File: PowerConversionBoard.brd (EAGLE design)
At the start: 152.4 x 101.6 mm, 46 parts, among them U1 LM2678, U2 LM2678

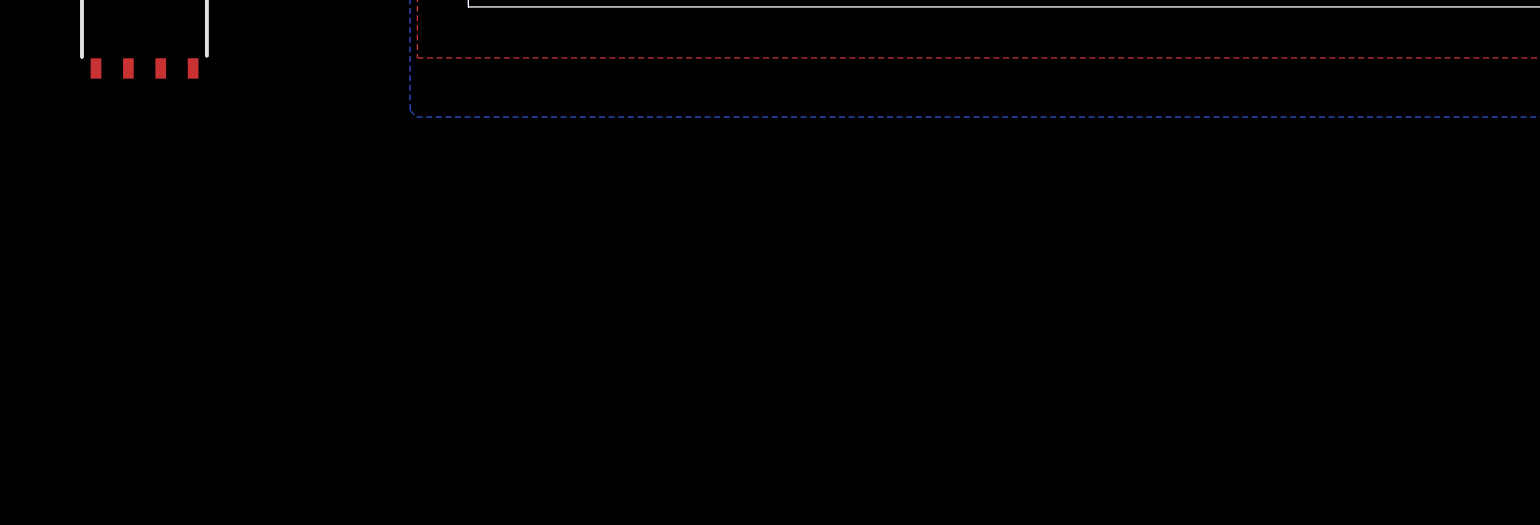
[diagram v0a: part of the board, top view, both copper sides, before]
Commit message: added the power ditribution connector
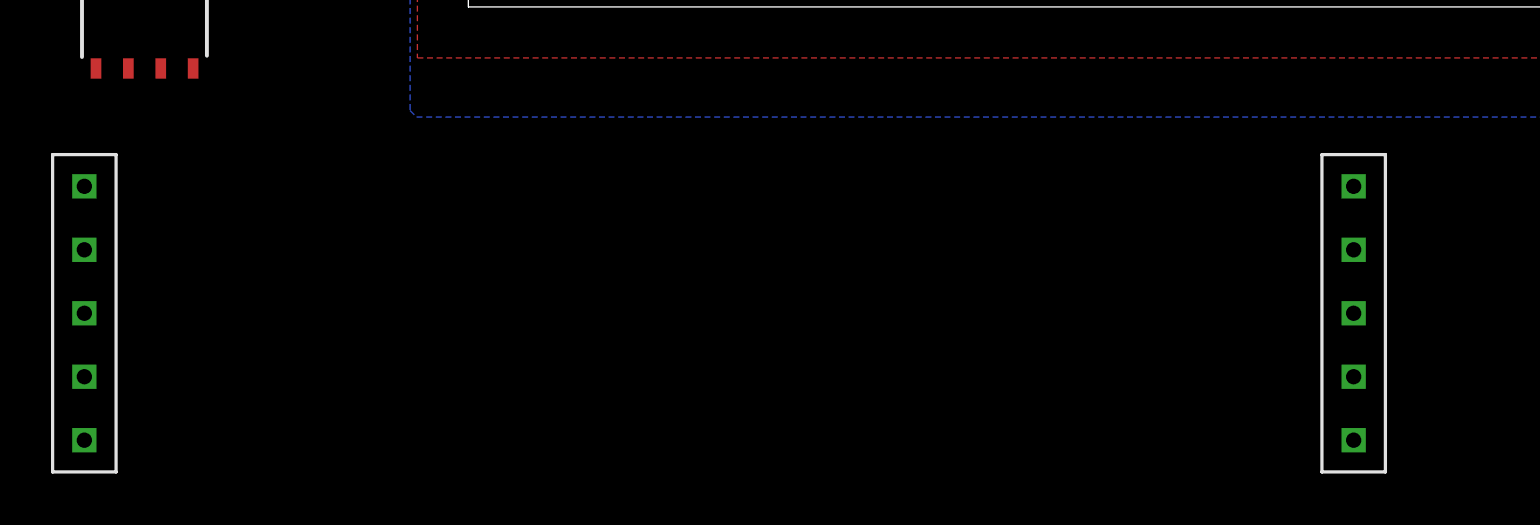
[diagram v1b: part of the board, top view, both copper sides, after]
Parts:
- added U$4: DIST_TO_CONV, Dist_To_Conv_Connector:DIST_TO_CONV
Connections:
- net +3.3V: now also U$4.3V
- net +48V: now also U$4.48V
- net +5V_3.3V: now also U$4.5V_1, U$4.5V_2, U$4.5V_3, U$4.5V_4
- net GND: now also U$4.GND_1, U$4.GND_2, U$4.GND_3, U$4.GND_4
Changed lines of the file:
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@@
 <attribute name="VALUE" x="-15.875" y="-4.953" size="1.778" layer="27"/>
 </element>
+<element name="U$4" library="Dist_To_Conv_Connector" package="DIST_TO_CONV" value="DIST_TO_CONV" x="-12.573" y="-9.525" smashed="yes"/>
 </elements>
 <signals>
@@
 <via x="105.41" y="36.576" extent="1-16" drill="0.9"/>
 <contactref element="U$6" pad="3"/>
+<contactref element="U$4" pad="GND_3"/>
+<contactref element="U$4" pad="GND_4"/>
+<contactref element="U$4" pad="GND_1"/>
+<contactref element="U$4" pad="GND_2"/>
 <wire x1="141.0716" y1="82.7906" x2="146.2532" y2="81.6356" width="0" layer="19" extent="1-1"/>
 <wire x1="132.715" y1="81.3698" x2="141.0716" y2="82.7906" width="0" layer="19" extent="1-1"/>
@@
 <wire x1="56.896" y1="3.302" x2="41.656" y2="3.048" width="0" layer="19" extent="1-1"/>
 <wire x1="-12.065" y1="-2.413" x2="3.81" y2="4.318" width="0" layer="19" extent="1-1"/>
+<wire x1="-15.0622" y1="-14.5034" x2="-12.065" y2="-2.413" width="0" layer="19" extent="1-1"/>
+<wire x1="-15.0622" y1="-16.9926" x2="-15.0622" y2="-14.5034" width="0" layer="19" extent="1-1"/>
+<wire x1="34.7218" y1="-14.5034" x2="33.528" y2="3.302" width="0" layer="19" extent="1-1"/>
+<wire x1="34.7218" y1="-16.9926" x2="34.7218" y2="-14.5034" width="0" layer="19" extent="1-1"/>
 <wire x1="78.232" y1="3.302" x2="56.896" y2="3.302" width="0" layer="19" extent="1-1"/>
 </signal>
@@
 <contactref element="U$6" pad="1"/>
 <contactref element="U$6" pad="2"/>
+<contactref element="U$4" pad="3V"/>
 <wire x1="-13.335" y1="-2.413" x2="124.3312" y2="84.9612" width="0" layer="19" extent="1-1"/>
 <wire x1="-14.605" y1="-2.413" x2="-13.335" y2="-2.413" width="0" layer="19" extent="1-1"/>
+<wire x1="-15.0622" y1="-7.0358" x2="-14.605" y2="-2.413" width="0" layer="19" extent="1-1"/>
 </signal>
 <signal name="N$2">
@@
 <contactref element="U$6" pad="8"/>
 <contactref element="U$6" pad="5"/>
+<contactref element="U$4" pad="5V_1"/>
+<contactref element="U$4" pad="5V_2"/>
+<contactref element="U$4" pad="5V_3"/>
+<contactref element="U$4" pad="5V_4"/>
 <wire x1="96.012" y1="96.012" x2="103.0224" y2="96.393" width="0" layer="19" extent="1-1"/>
 <wire x1="83.1986" y1="91.5416" x2="96.012" y2="96.012" width="0" layer="19" extent="1-1"/>
-<wire x1="-10.795" y1="2.787" x2="46.9138" y2="83.4898" width="0" layer="19" extent="1-1"/>
+<wire x1="34.7218" y1="-9.525" x2="46.9138" y2="83.4898" width="0" layer="19" extent="1-1"/>
+<wire x1="34.7218" y1="-12.0142" x2="34.7218" y2="-9.525" width="0" layer="19" extent="1-1"/>
+<wire x1="-10.795" y1="2.787" x2="34.7218" y2="-9.525" width="0" layer="19" extent="1-1"/>
 <wire x1="-14.605" y1="2.787" x2="-10.795" y2="2.787" width="0" layer="19" extent="1-1"/>
+<wire x1="-15.0622" y1="-9.525" x2="-14.605" y2="2.787" width="0" layer="19" extent="1-1"/>
+<wire x1="-15.0622" y1="-12.0142" x2="-15.0622" y2="-9.525" width="0" layer="19" extent="1-1"/>
 </signal>
 <signal name="N$3">
@@
 <wire x1="52.07" y1="85.852" x2="44.45" y2="93.472" width="1.27" layer="16"/>
 <wire x1="44.45" y1="93.472" x2="43.18" y2="93.472" width="1.27" layer="16"/>
+<contactref element="U$4" pad="48V"/>
 <wire x1="43.18" y1="93.472" x2="42.9514" y2="91.7058" width="0" layer="19" extent="16-16"/>
 <wire x1="38.227" y1="93.8726" x2="43.18" y2="93.472" width="0" layer="19" extent="16-16"/>
@@
 <wire x1="4.6736" y1="96.8756" x2="10.2616" y2="96.6352" width="0" layer="19" extent="1-1"/>
 <wire x1="4.9784" y1="89.3572" x2="4.6736" y2="96.8756" width="0" layer="19" extent="1-1"/>
+<wire x1="34.7218" y1="-7.0358" x2="51.9938" y2="83.4898" width="0" layer="19" extent="1-1"/>
 </signal>
 </signals>

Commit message: Align schematic to 0.1 in. Create board with dimension
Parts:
- U$2, U$7: value HCM1305 -> HCMA1305; device HCM1305:HCM1305 -> Inductor_15uH - hcma1305:HCMA1305
- moved D1 221.0 mm to (-69.8, 76.2), turned to 0 degrees
- moved +3.3V 210.3 mm to (-57.1, 47.0)
- moved R2 209.7 mm to (-58.4, 76.2), turned to 0 degrees
- moved +5V 209.3 mm to (-63.5, 47.0)
- moved R3 204.5 mm to (-62.2, 76.2), turned to 0 degrees
- moved GND3 177.2 mm to (-29.2, 57.1)
- moved R4 174.7 mm to (-41.9, 76.2), turned to 0 degrees
- moved 5V_3.3 173.0 mm to (-69.8, 47.0)
- moved U$13 172.1 mm to (-36.8, 57.1), turned to 0 degrees
- moved 5V 171.5 mm to (-25.4, 47.0)
- moved +3.3 166.1 mm to (-19.1, 47.0)
- moved R1 163.8 mm to (-54.6, 76.2), turned to 0 degrees
- moved 5V_3.3_TP 163.5 mm to (-48.3, 34.3)
- moved D3 156.3 mm to (-15.2, 82.5), turned to 0 degrees
- moved C12 153.0 mm to (-67.3, 57.1), turned to 0 degrees
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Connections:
- net +12V renamed N$11
- net +5V: now also U$2.P$2; no longer U$2.2, U1.6
- net +5V_3.3V: now also U$7.P$2; no longer U$7.2
- net N$1: now also U$2.P$1, U1.6; no longer U$2.1
- net N$7: now also U$7.P$1; no longer U$7.1
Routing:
- net +5V: track 116.5 -> 0.00 mm, vias 7 -> 0
- net +5V_3.3V: track 54.9 -> 0.00 mm
- net +3.3V: track 34.7 -> 0.00 mm, vias 5 -> 0
- net N$1: track 33.5 -> 0.00 mm
- net GND: track 28.2 -> 0.00 mm, vias 67 -> 0
- net N$7: track 28.0 -> 0.00 mm
- net +48V: track 15.8 -> 0.00 mm, vias 2 -> 0
- net N$2: track 9.97 -> 0.00 mm
- net N$14: track 9.64 -> 0.00 mm
- net N$11: track 9.27 -> 0.00 mm, vias 1 -> 0
- net N$5: track 2.95 -> 0.00 mm
- net N$6: track 2.88 -> 0.00 mm
- net N$10: track 2.87 -> 0.00 mm
- net N$8: track 2.24 -> 0.00 mm
- net N$4: track 1.93 -> 0.00 mm
- removed copper zone on layer 16, net +3.3V
- removed copper zone on layer 1, net +5V
- removed copper zone on layer 16, net +5V
- removed copper zone on layer 1, net +5V_3.3V
- removed copper zone on layer 1, net CUT
- removed copper zone on layer 16, net CUT
- removed copper zone on layer 16, net CUTG
- removed copper zone on layer 1, net GND
- removed copper zone on layer 16, net GND
- removed copper zone on layer 1, net GNDCUT
- removed copper zone on layer 16, net N$11
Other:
- board size 152.4 x 101.6 mm -> 72.4 x 71.1 mm
- board text removed: "Power Conversion v1 Guillermo Martinez Erin Park Ryan Pearson Cynthia Zatlokowicz"
- board text removed: "owo"

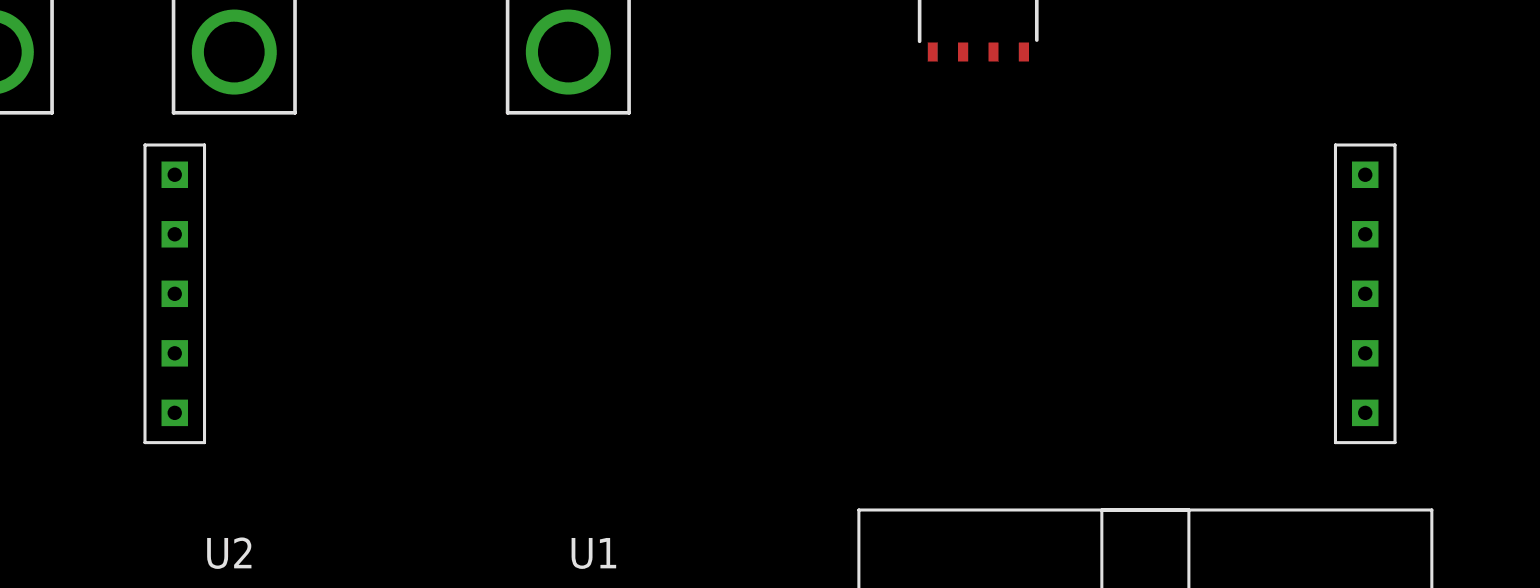
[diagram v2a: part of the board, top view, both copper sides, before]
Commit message: Added the connector to the distribution board
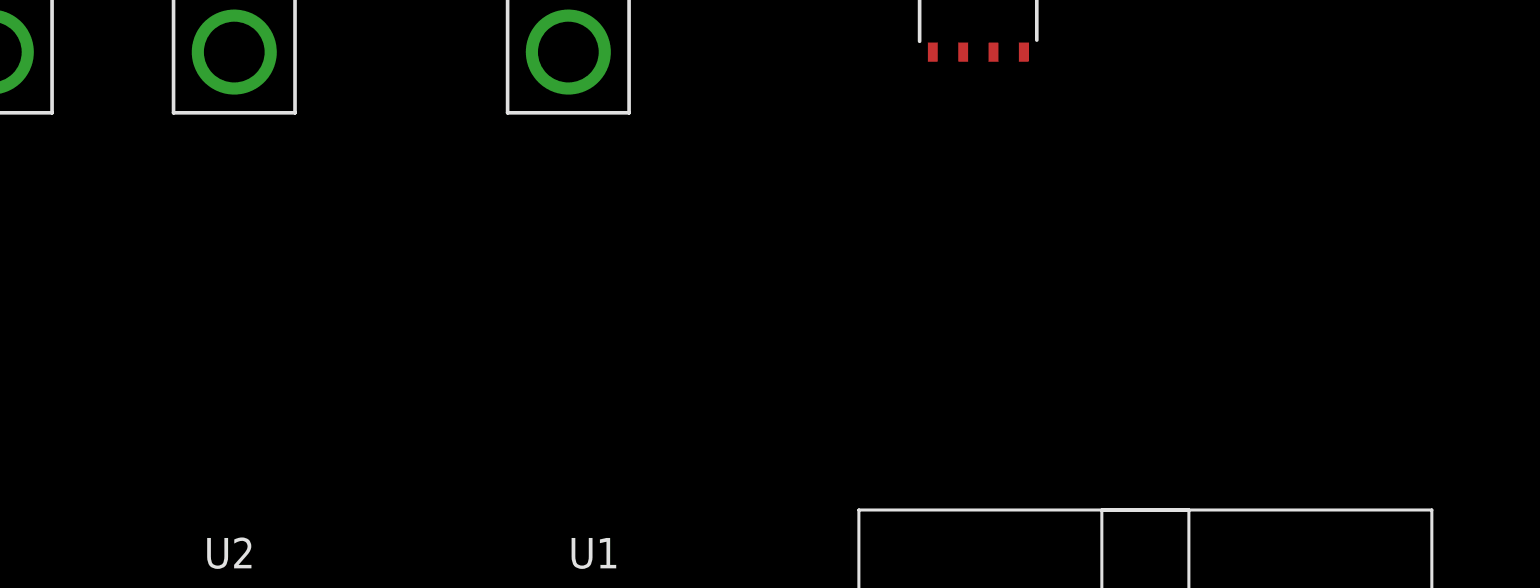
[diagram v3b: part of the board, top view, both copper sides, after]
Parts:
- removed U$4: DIST_TO_CONV, Dist_To_Conv_Connector:DIST_TO_CONV
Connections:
- net +3.3V: no longer U$4.3V
- net +48V: no longer U$4.48V
- net +5V_3.3V: no longer U$4.5V_1, U$4.5V_2, U$4.5V_3, U$4.5V_4
- net GND: no longer U$4.GND_1, U$4.GND_2, U$4.GND_3, U$4.GND_4
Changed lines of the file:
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@@
 <attribute name="NAME" x="-47.29" y="50.69" size="1.27" layer="25"/>
 </element>
-<element name="U$4" library="Dist_To_Conv_Connector" package="DIST_TO_CONV" value="DIST_TO_CONV" x="-62.23" y="26.67" smashed="yes"/>
 <element name="U$6" library="5-33Regulator" package="VOLTAGEREGULATOR" value="5-33REGULATOR" x="-33.02" y="34.29" smashed="yes">
 <attribute name="NAME" x="-34.29" y="40.64" size="1.778" layer="25"/>
@@
 <contactref element="D1" pad="C"/>
 <contactref element="D2" pad="C"/>
-<contactref element="U$4" pad="GND_3"/>
-<contactref element="U$4" pad="GND_4"/>
-<contactref element="U$4" pad="GND_1"/>
-<contactref element="U$4" pad="GND_2"/>
 <contactref element="C12" pad="-"/>
 <contactref element="U$1" pad="P$1"/>
@@
 <wire x1="-68.973" y1="76.2" x2="-61.55" y2="71.12" width="0" layer="19" extent="1-1"/>
 <wire x1="-72.783" y1="76.2" x2="-68.973" y2="76.2" width="0" layer="19" extent="1-1"/>
-<wire x1="-14.9352" y1="21.6916" x2="-30.48" y2="34.29" width="0" layer="19" extent="1-1"/>
-<wire x1="-14.9352" y1="19.2024" x2="-14.9352" y2="21.6916" width="0" layer="19" extent="1-1"/>
 <wire x1="-62.23" y1="34.29" x2="-42.91" y2="44.705" width="0" layer="19" extent="1-1"/>
-<wire x1="-64.7192" y1="21.6916" x2="-62.23" y2="34.29" width="0" layer="19" extent="1-1"/>
-<wire x1="-64.7192" y1="19.2024" x2="-64.7192" y2="21.6916" width="0" layer="19" extent="1-1"/>
-<wire x1="-58.42" y1="6.35" x2="-64.7192" y2="19.2024" width="0" layer="19" extent="1-1"/>
+<wire x1="-58.42" y1="6.35" x2="-62.23" y2="34.29" width="0" layer="19" extent="1-1"/>
 <wire x1="-50.0888" y1="6.35" x2="-58.42" y2="6.35" width="0" layer="19" extent="1-1"/>
 <wire x1="-43.18" y1="6.35" x2="-50.0888" y2="6.35" width="0" layer="19" extent="1-1"/>
@@
 <contactref element="+3.3V" pad="P$1"/>
 <contactref element="+3.3" pad="P$1"/>
-<contactref element="U$4" pad="3V"/>
-<wire x1="-57.15" y1="46.99" x2="-64.7192" y2="29.1592" width="0" layer="19" extent="1-1"/>
-<wire x1="-37.63" y1="57.15" x2="-57.15" y2="46.99" width="0" layer="19" extent="1-1"/>
-<wire x1="-19.05" y1="46.99" x2="-37.63" y2="57.15" width="0" layer="19" extent="1-1"/>
 <wire x1="-31.75" y1="34.29" x2="-19.05" y2="46.99" width="0" layer="19" extent="1-1"/>
 <wire x1="-33.02" y1="34.29" x2="-31.75" y2="34.29" width="0" layer="19" extent="1-1"/>
+<wire x1="-37.63" y1="57.15" x2="-19.05" y2="46.99" width="0" layer="19" extent="1-1"/>
+<wire x1="-57.15" y1="46.99" x2="-37.63" y2="57.15" width="0" layer="19" extent="1-1"/>
 <wire x1="-61.38" y1="76.2" x2="-57.15" y2="46.99" width="0" layer="19" extent="1-1"/>
 </signal>
@@
 <contactref element="5V_3.3" pad="P$1"/>
 <contactref element="5V_3.3_TP" pad="P$1"/>
-<contactref element="U$4" pad="5V_1"/>
-<contactref element="U$4" pad="5V_2"/>
-<contactref element="U$4" pad="5V_3"/>
-<contactref element="U$4" pad="5V_4"/>
 <wire x1="-33.7" y1="71.12" x2="-22.27" y2="71.12" width="0" layer="19" extent="1-1"/>
 <wire x1="-45.13" y1="71.12" x2="-33.7" y2="71.12" width="0" layer="19" extent="1-1"/>
@@
 <wire x1="-29.21" y1="39.49" x2="-33.02" y2="39.49" width="0" layer="19" extent="1-1"/>
 <wire x1="-48.26" y1="34.29" x2="-33.02" y2="39.49" width="0" layer="19" extent="1-1"/>
-<wire x1="-64.7192" y1="26.67" x2="-48.26" y2="34.29" width="0" layer="19" extent="1-1"/>
-<wire x1="-64.7192" y1="24.1808" x2="-64.7192" y2="26.67" width="0" layer="19" extent="1-1"/>
-<wire x1="-14.9352" y1="26.67" x2="-29.21" y2="39.49" width="0" layer="19" extent="1-1"/>
-<wire x1="-14.9352" y1="24.1808" x2="-14.9352" y2="26.67" width="0" layer="19" extent="1-1"/>
-<wire x1="-23.71" y1="8.89" x2="-14.9352" y2="24.1808" width="0" layer="19" extent="1-1"/>
-<wire x1="-69.85" y1="46.99" x2="-64.7192" y2="26.67" width="0" layer="19" extent="1-1"/>
-<wire x1="-50.0888" y1="8.89" x2="-64.7192" y2="24.1808" width="0" layer="19" extent="1-1"/>
+<wire x1="-69.85" y1="46.99" x2="-48.26" y2="34.29" width="0" layer="19" extent="1-1"/>
+<wire x1="-50.0888" y1="8.89" x2="-48.26" y2="34.29" width="0" layer="19" extent="1-1"/>
+<wire x1="-23.71" y1="8.89" x2="-50.0888" y2="8.89" width="0" layer="19" extent="1-1"/>
 </signal>
 <signal name="N$4">
@@
 <contactref element="C3" pad="1"/>
 <contactref element="U2" pad="2"/>
-<contactref element="U$4" pad="48V"/>
 <wire x1="-31.33" y1="77.47" x2="-22.27" y2="77.47" width="0" layer="19" extent="1-1"/>
 <wire x1="-22.27" y1="64.77" x2="-22.27" y2="77.47" width="0" layer="19" extent="1-1"/>
@@
 <wire x1="-65.19" y1="76.2" x2="-56.56" y2="71.12" width="0" layer="19" extent="1-1"/>
 <wire x1="-67.99" y1="71.12" x2="-65.19" y2="76.2" width="0" layer="19" extent="1-1"/>
-<wire x1="-14.9352" y1="29.1592" x2="-16.51" y2="57.15" width="0" layer="19" extent="1-1"/>
 <wire x1="-72.39" y1="34.29" x2="-67.99" y2="71.12" width="0" layer="19" extent="1-1"/>
 <wire x1="-50.0888" y1="3.81" x2="-72.39" y2="34.29" width="0" layer="19" extent="1-1"/>
